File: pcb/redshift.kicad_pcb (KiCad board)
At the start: 4 copper layers, 45 x 63.5 mm, 45 parts, among them IC1 LPC5516JEV98, J1 USB_C_Receptacle_USB2.0, J2 Side, J3 Conn_01x06_Female, SW1 SW_SPDT, SW2 SW_SPDT, SW3 SW_SPD, U1 PAW 3399, U2 MIC5350-SGYMT-TR

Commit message: pre v0.1
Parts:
- removed U2: MIC5350-SGYMT-TR, Package_DFN_QFN:Micrel_MLF-8-1EP_2x2mm_P0.5mm_EP0.8x1.3mm_ThermalVias
- added C17: 100nF, Capacitor_SMD:C_0402_1005Metric, F.Cu at (144.8, 103.0)
- added C18: 4.7uF, Capacitor_SMD:C_0402_1005Metric, F.Cu at (144.8, 104.0)
- added C19: 100nF, Capacitor_SMD:C_0402_1005Metric, F.Cu at (144.8, 108.2)
- added C20: 33uF, Capacitor_SMD:C_0402_1005Metric, F.Cu at (144.8, 109.2)
- added C21: 100nF, Capacitor_SMD:C_0402_1005Metric, F.Cu at (144.8, 107.2)
- added C22: 4.7uF, Capacitor_SMD:C_0402_1005Metric, F.Cu at (144.8, 106.2)
- added C23: 0.1uF, Capacitor_SMD:C_0201_0603Metric, F.Cu at (142.8, 85.8)
- added C24: 100nF, Capacitor_SMD:C_0402_1005Metric, F.Cu at (143.3, 93.5)
- added R10: 10k, Resistor_SMD:R_0402_1005Metric, F.Cu at (155.2, 106.5)
- added R11: 10k, Resistor_SMD:R_0402_1005Metric, F.Cu at (155.2, 107.5)
- added R12: 10k, Resistor_SMD:R_0402_1005Metric, F.Cu at (155.2, 110.5)
- added R8: 10k, Resistor_SMD:R_0402_1005Metric, F.Cu at (129.8, 105.5)
- added R9: 10k, Resistor_SMD:R_0402_1005Metric, F.Cu at (155.2, 105.5)
- added TP1: TestPoint, TestPoint:TestPoint_Pad_D1.5mm, B.Cu at (127.0, 102.5)
- added TP10: TestPoint, TestPoint:TestPoint_Pad_D1.5mm, B.Cu at (149.5, 77.5)
- added TP11: TestPoint, TestPoint:TestPoint_Pad_D1.5mm, B.Cu at (149.5, 82.5)
- added TP12: TestPoint, TestPoint:TestPoint_Pad_D1.5mm, B.Cu at (149.0, 114.5)
- added TP13: TestPoint, TestPoint:TestPoint_Pad_D1.5mm, B.Cu at (122.5, 81.0)
- added TP14: TestPoint, TestPoint:TestPoint_Pad_D1.5mm, B.Cu at (152.5, 114.5)
- added TP15: TestPoint, TestPoint:TestPoint_Pad_D1.5mm, B.Cu at (122.5, 78.0)
- added TP16: TestPoint, TestPoint:TestPoint_Pad_D1.5mm, B.Cu at (152.5, 111.0)
- added TP17: TestPoint, TestPoint:TestPoint_Pad_D1.5mm, B.Cu at (147.8, 69.2)
- added TP2: TestPoint, TestPoint:TestPoint_Pad_D1.5mm, B.Cu at (119.0, 75.5)
- added TP3: TestPoint, TestPoint:TestPoint_Pad_D1.5mm, B.Cu at (127.0, 100.0)
- added TP4: TestPoint, TestPoint:TestPoint_Pad_D1.5mm, B.Cu at (119.0, 80.5)
- added TP5: TestPoint, TestPoint:TestPoint_Pad_D1.5mm, B.Cu at (127.0, 106.0)
- added TP6: TestPoint, TestPoint:TestPoint_Pad_D1.5mm, B.Cu at (156.5, 80.5)
- added TP7: TestPoint, TestPoint:TestPoint_Pad_D1.5mm, B.Cu at (156.5, 85.5)
- added TP8: TestPoint, TestPoint:TestPoint_Pad_D1.5mm, B.Cu at (122.5, 75.2)
- added TP9: TestPoint, TestPoint:TestPoint_Pad_D1.5mm, B.Cu at (126.0, 75.2)
- added U3: TCR2LE19,LM(CT, Package_TO_SOT_SMD:SOT-553, F.Cu at (148.0, 107.0)
- added U4: MIC5528-3.3YMT-TR, MIC5528-3:SON40P120X120X60-7N, F.Cu at (142.0, 66.8)
- added Y1: XRCGB16M000FXN16R0, Crystal:Crystal_SMD_2016-4Pin_2.0x1.6mm, F.Cu at (143.3, 87.5)
- added kibuzzard-61C38E31: G***, kibuzzard-61C38E31, B.Cu at (150.8, 95.5)
- added kibuzzard-61C38F6A: G***, kibuzzard-61C38F6A, B.Cu at (150.8, 102.0)
- C10: value 0.1uF -> 2.2uF
- C15: value 100nF -> 0.1uF; footprint Capacitor_SMD:C_0402_1005Metric -> Capacitor_SMD:C_0201_0603Metric
- C2, C7: value 2.2uF -> 0.1uF
- SW1, SW2: value SW_SPDT -> SW_SP
- SW3: value SW_SPD -> SW_SP
- U1: value PAW 3399 -> PAW3399DM‐T4QU
- moved C7 41.1 mm to (147.8, 108.8)
- moved C2 36.8 mm to (147.7, 105.2)
- moved C15 18.8 mm to (145.0, 88.2), turned to 90 degrees
- moved C10 6.58 mm to (143.8, 66.8), turned to 90 degrees
- moved C8 4.50 mm to (140.0, 66.7), turned to -90 degrees
- moved C9 0.75 mm to (138.8, 88.0)
- moved C16 0.27 mm to (143.2, 92.5)
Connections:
- C10 pad 1: /BYP -> +3V3
- C15 pad 1: +3V3 -> /XTAL+
- C8 pad 1: +3V3 -> +5V
- D1 pad 2: /USB_D+ -> /USB_D-
- D1 pad 3: /USB_D- -> /USB_D+
- IC1 pad E6: unconnected-(IC1-PadE6) -> /SNSR_MTN
- IC1 pad N3: GND -> /XTAL+
- U1 pad 14: (no net) -> /SNSR_RST
- U1 pad 3: unconnected-(U1-Pad3) -> GND
- U1 pad 4: +1V8 -> Net-(C19-Pad1)
- U1 pad 5: +3V3 -> Net-(C21-Pad1)
- U1 pad 7: /SNSR_RST -> Net-(C17-Pad2)
- U1 pad 9: unconnected-(U1-Pad9) -> /SNSR_MTN
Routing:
- net +5V: track 12.8 -> 56.3 mm, vias 0 -> 3
- net +1V8: track 47.8 -> 13.3 mm
- net /SNSR_MTN: track 0.00 -> 14.8 mm, vias 0 -> 1
- net /SNSR_RST: track 11.8 -> 21.8 mm
- net /XTAL-: track 0.00 -> 8.41 mm
- net /XTAL+: track 0.00 -> 7.41 mm
- net /SW1_L_NO: track 30.5 -> 35.2 mm
- net /SWO: track 25.0 -> 29.3 mm, vias 1 -> 2
- net GND: track 34.6 -> 38.9 mm, vias 30 -> 37
- net /FC6_MOSI: track 16.6 -> 20.8 mm, vias 1 -> 2
- net /ENC_A: track 32.4 -> 36.5 mm
- net /FC6_SCK: track 18.4 -> 22.5 mm, vias 2 -> 3
- net /FC6_MISO: track 20.0 -> 24.1 mm, vias 2 -> 3
- net /SW1_L_NC: track 26.2 -> 29.4 mm
- net /SWCLK: track 25.0 -> 27.9 mm, vias 2 -> 1
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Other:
- board text added: "CERN-OHL-P v2 github.com Dekanova/redshift"

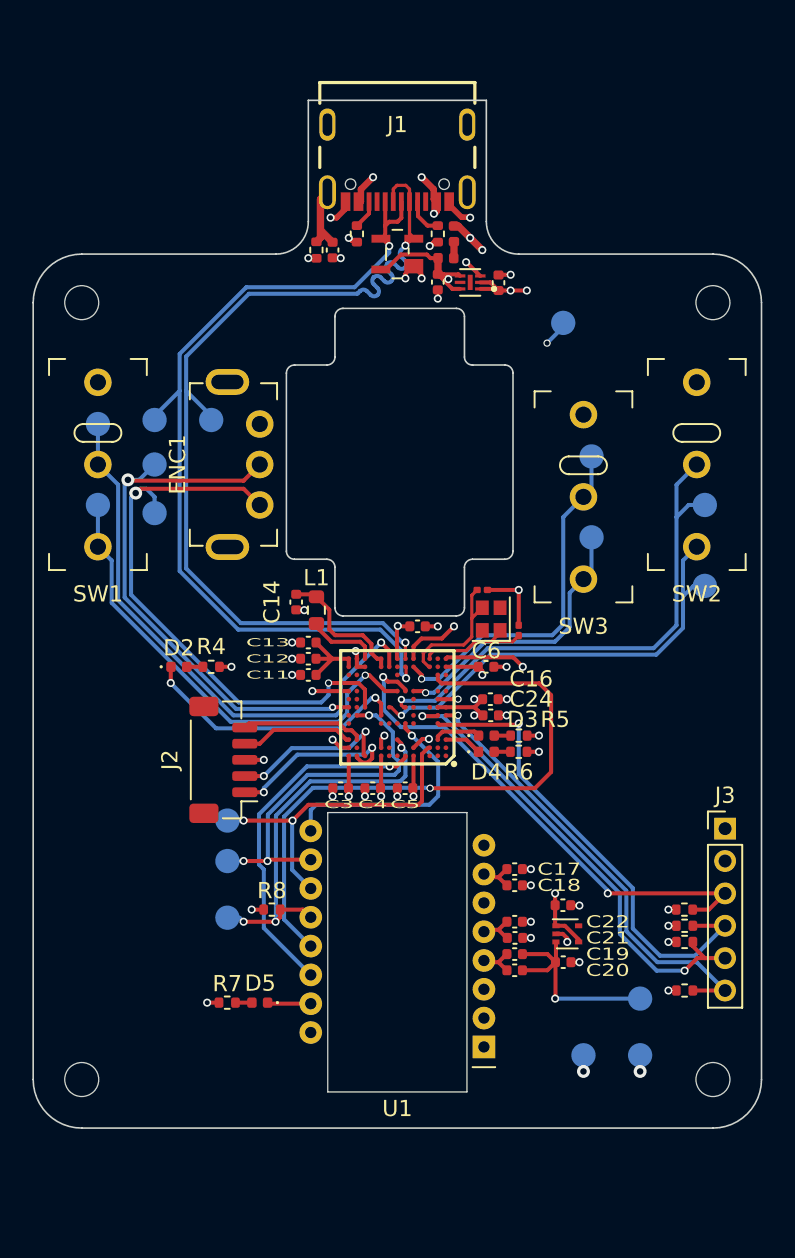
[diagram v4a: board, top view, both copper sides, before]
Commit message: add lpc55 footprint from solokeys, release v0.1
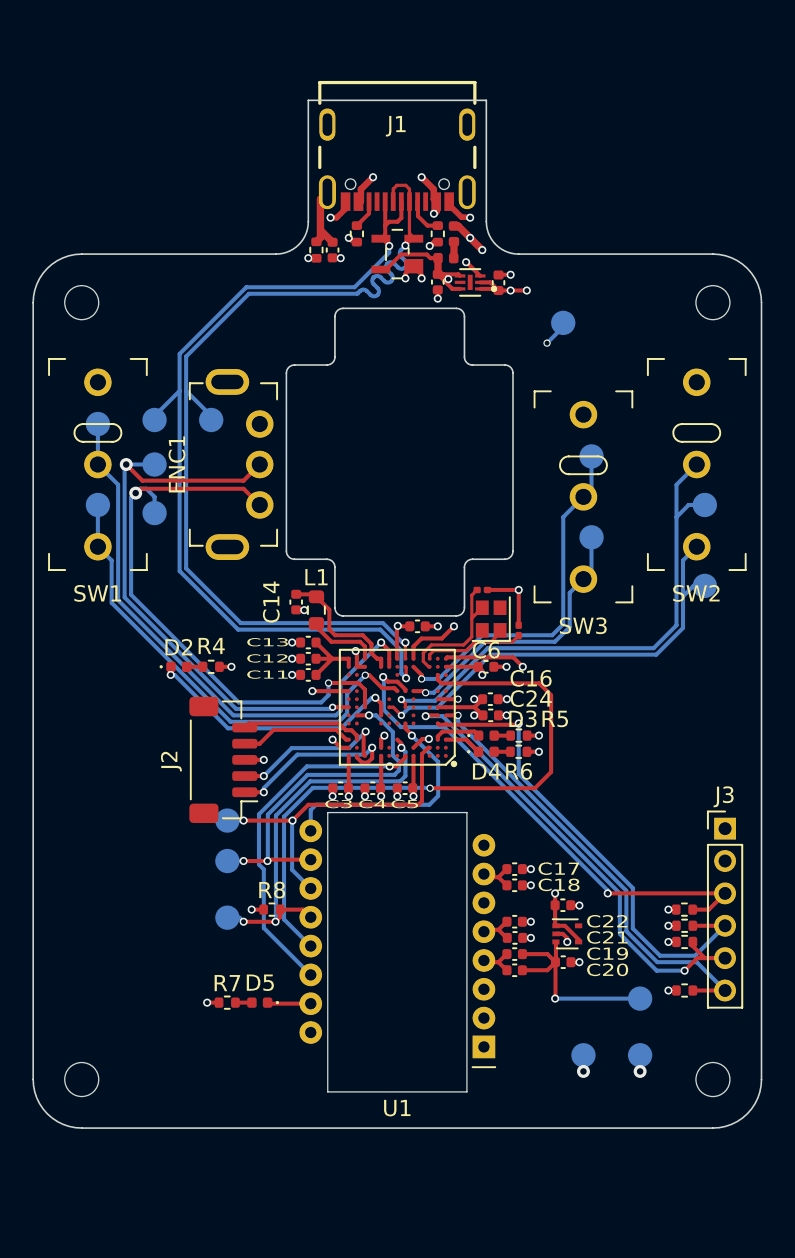
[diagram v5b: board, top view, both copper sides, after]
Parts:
- IC1: footprint dekanova:BGA98C50P13X13_700X700X97 -> solokeys:BGA98C50P13X13_700X700X97N
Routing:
- net /ENC_B: track 34.7 -> 35.8 mm

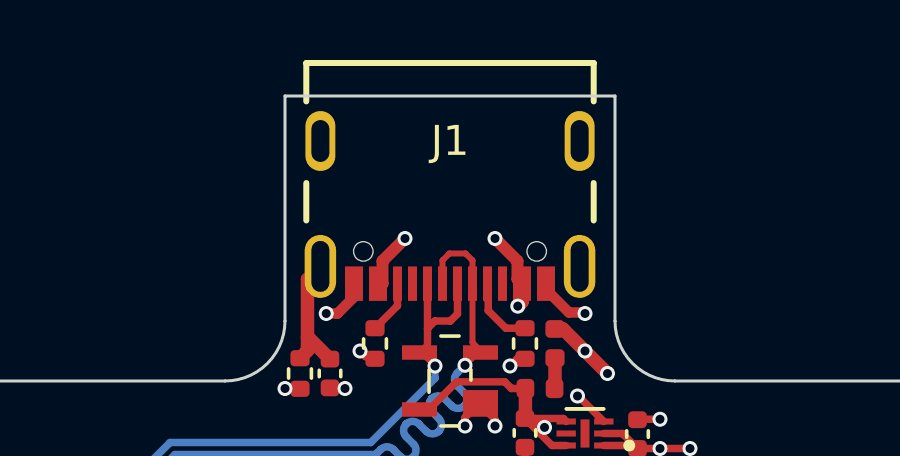
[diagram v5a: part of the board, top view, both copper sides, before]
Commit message: Add GCT usb-C 2.0 port footprint to local project
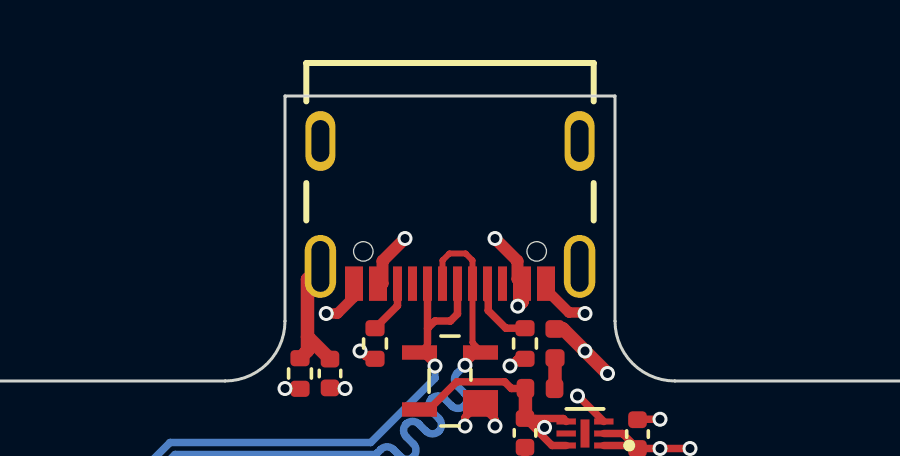
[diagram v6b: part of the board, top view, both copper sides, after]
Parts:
- J1: footprint dekanova:GCT_USB4105-GF-A -> GCT_USB:GCT_USB4105-GF-A

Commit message: add ISP pin
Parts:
- added TP18: TestPoint, TestPoint:TestPoint_Pad_D1.5mm, B.Cu at (139.0, 96.8)
- C15, C23: value 0.1uF -> 12pF
- C18: value 4.7uF -> 10uF
- C20: value 33uF -> 22uF
- R4, R5, R6, R7: value 100R -> 10k
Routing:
- net /SNSR_MTN: track 14.8 -> 16.8 mm
- net /ISP: track 0.00 -> 1.50 mm, vias 0 -> 1
- net /SNSR_RST: track 21.8 -> 23.1 mm, vias 1 -> 3
- net +3V3: track 28.5 -> 29.7 mm
- net /FC6_SCK: track 22.5 -> 21.5 mm
- net /FC6_MISO: track 24.1 -> 23.1 mm
- net /FC6_MOSI: track 20.8 -> 21.3 mm

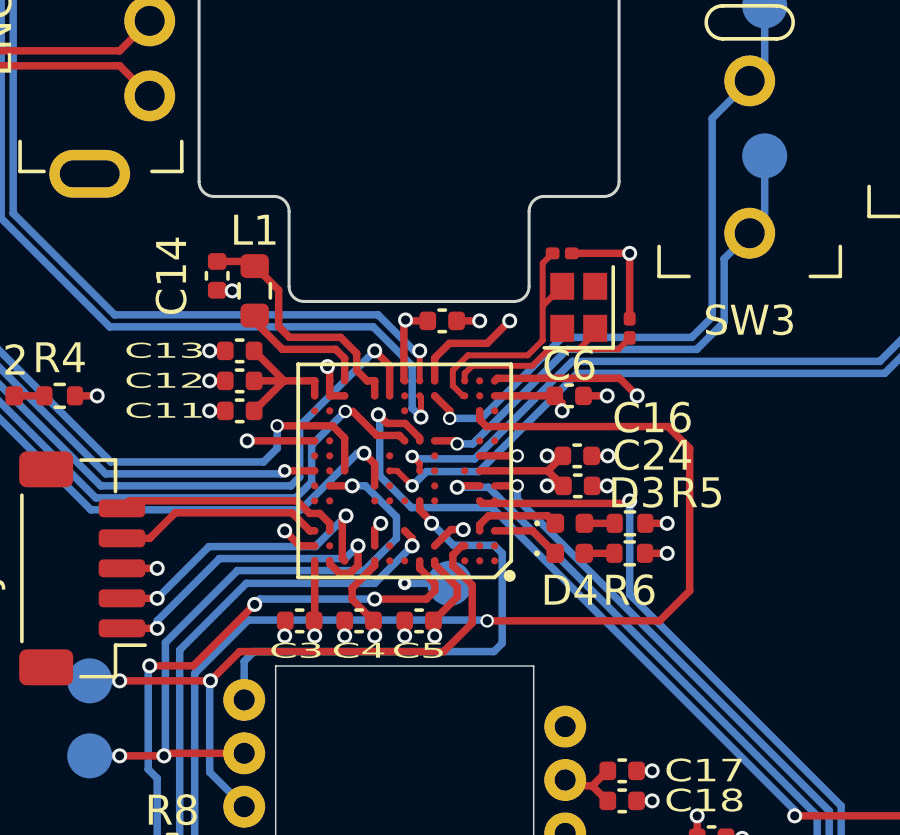
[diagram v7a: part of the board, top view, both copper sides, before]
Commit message: fix #2, add missing lib source
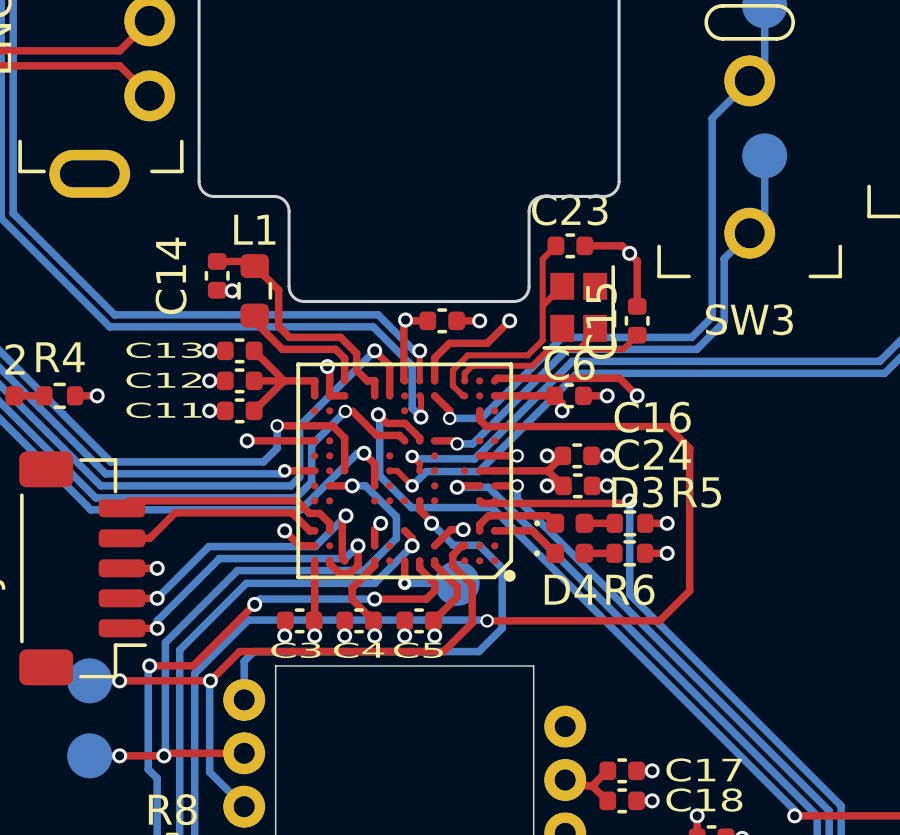
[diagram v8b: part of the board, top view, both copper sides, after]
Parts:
- C15, C23: footprint Capacitor_SMD:C_0201_0603Metric -> Capacitor_SMD:C_0402_1005Metric
- IC1: value LPC5516JEV98 -> LPC5526JEV98
- moved C23 0.37 mm to (143.0, 85.5)
- moved C15 0.35 mm to (145.2, 88.0)
- moved TP18 0.25 mm to (139.2, 96.8)
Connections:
- IC1 pad A7: unconnected-(IC1-PadA7) -> /ISP
- IC1 pad E1: (no net) -> unconnected-(IC1-PadE1)
- IC1 pad E12: (no net) -> unconnected-(IC1-PadE12)
- IC1 pad F8: (no net) -> unconnected-(IC1-PadF8)
- IC1 pad H8: (no net) -> unconnected-(IC1-PadH8)
- IC1 pad N8: (no net) -> unconnected-(IC1-PadN8)
- U3 pad 5: (no net) -> unconnected-(U3-Pad5)
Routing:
- net /ISP: track 1.50 -> 2.50 mm
- net GND: track 38.9 -> 38.2 mm
- net /SNSR_MTN: track 16.8 -> 16.2 mm
